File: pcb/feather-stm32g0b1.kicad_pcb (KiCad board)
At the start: 4 copper layers, 50.8 x 22.9 mm, 55 parts, among them CN1 STDC14, CN2 SM04B-SRSS-TB (LF)(SN), CN3 ZX-PH2.0-WT2P, CN4 SM04B-SRSS-TB (LF)(SN), J1 Conn_01x12, J2 Conn_01x16, J3 GT-USB-7010ASV, Q1 DMG3415U-7, SW1 SW_Push, U1 STM32G0B1CBT6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

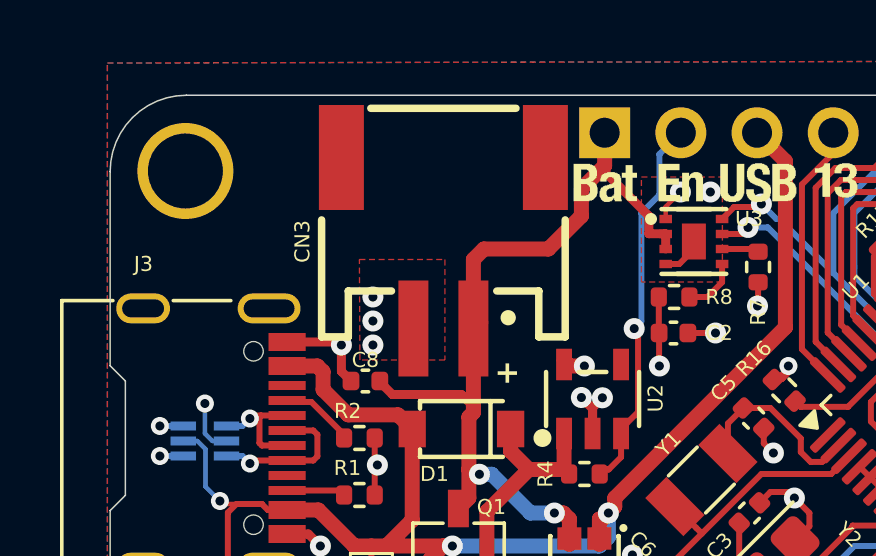
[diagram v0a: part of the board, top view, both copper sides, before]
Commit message: Upgraded kicad project to kicad 10
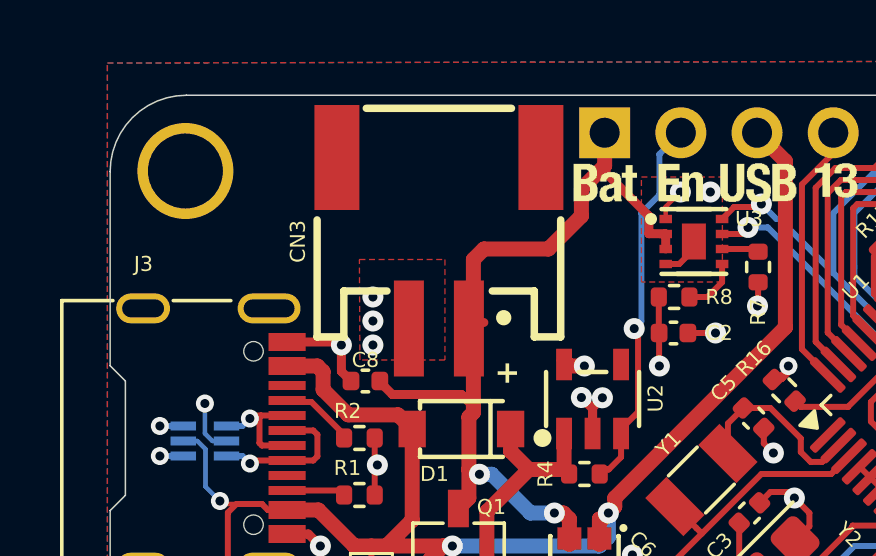
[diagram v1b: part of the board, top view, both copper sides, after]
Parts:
- moved CN3 0.15 mm to (111.0, 84.4)

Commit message: Used kibuzzard to generate nice labels for buttons, ports and leds
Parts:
- added kibuzzard-69DFDE44: G***, kibuzzard-69DFDE44, F.Cu at (134.2, 94.2)
- added kibuzzard-69DFDEC0: G***, kibuzzard-69DFDEC0, F.Cu at (141.8, 96.3)
- added kibuzzard-69DFDEEF: G***, kibuzzard-69DFDEEF, F.Cu at (141.7, 98.0)
- added kibuzzard-69DFDF04: G***, kibuzzard-69DFDF04, F.Cu at (102.1, 97.0)
- added kibuzzard-69DFDF67: G***, kibuzzard-69DFDF67, F.Cu at (140.6, 94.7)
- added kibuzzard-69DFDFA3: G***, kibuzzard-69DFDFA3, F.Cu at (106.3, 84.9)
- added kibuzzard-69DFDFE1: G***, kibuzzard-69DFDFE1, F.Cu at (146.7, 83.8)
- added kibuzzard-69DFDFEF: G***, kibuzzard-69DFDFEF, F.Cu at (146.7, 91.0)
- added kibuzzard-69DFE014: G***, kibuzzard-69DFE014, F.Cu at (141.6, 83.7)
- added kibuzzard-69DFE1A1: G***, kibuzzard-69DFE1A1, F.Cu at (136.8, 98.2)
- SW1: footprint Button_Switch_SMD:SW_SPST_B3U-1000P -> prop-devboard:WUERTH_434153017835
- moved C8 9.26 mm to (116.9, 84.9), turned to 90 degrees
- moved C10 4.79 mm to (131.2, 97.6), turned to 90 degrees
- moved R3 0.90 mm to (129.7, 97.6)
- moved SW1 0.35 mm to (134.2, 96.2), turned to 0 degrees
- moved R10 0.30 mm to (138.7, 98.0)
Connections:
- SW1 pad 1: GND -> NRST
- SW1 pad 2: NRST -> GND
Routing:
- net GND: track 48.4 -> 46.3 mm, vias 33 -> 34
- net VBAT: track 29.1 -> 27.1 mm
- net LED_USR: track 11.2 -> 12.8 mm
- net +3V3: track 112.2 -> 111.5 mm
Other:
- board text removed: "CHRG"
- board text removed: "I2C1"
- board text removed: "I2C2"
- board text removed: "I2C3"
- board text removed: "PWR"
- board text removed: "RESET"
- board text removed: "SPI2"
- board text removed: "USR"

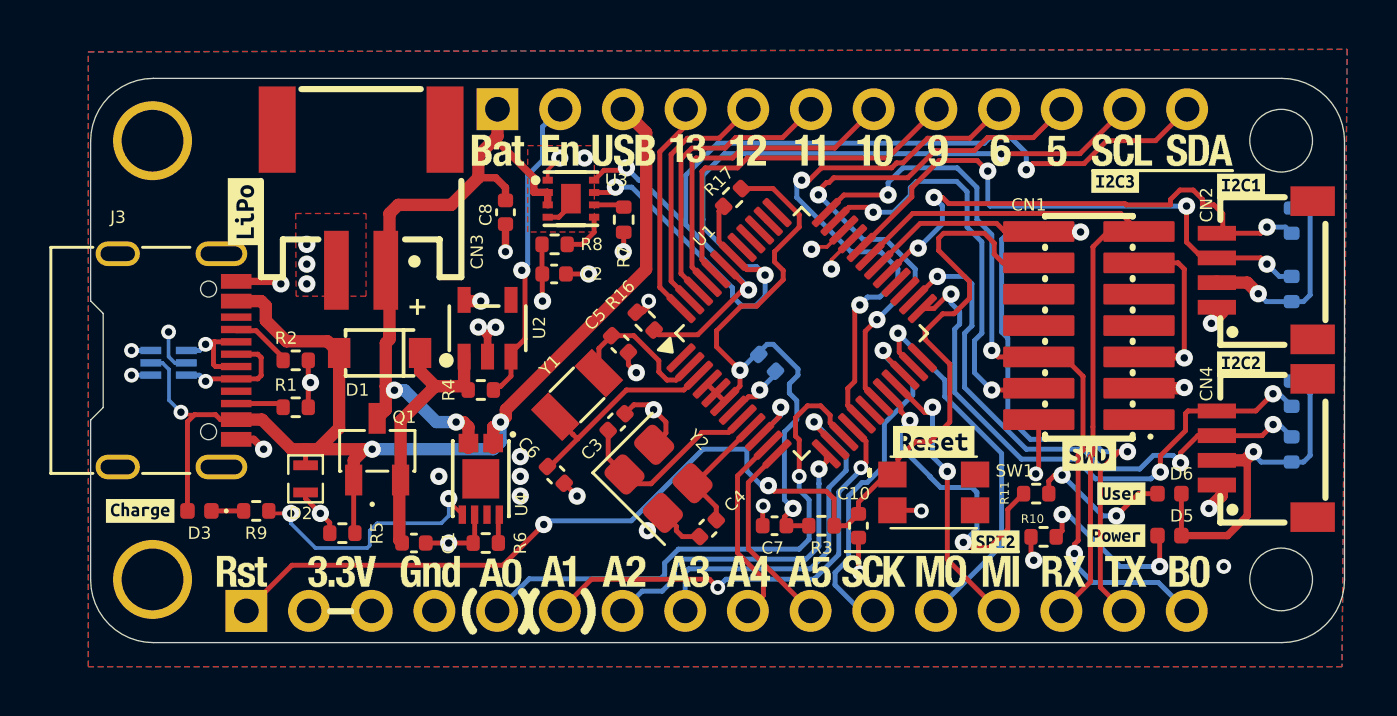
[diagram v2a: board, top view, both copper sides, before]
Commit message: Added I2C EEPROM to the board
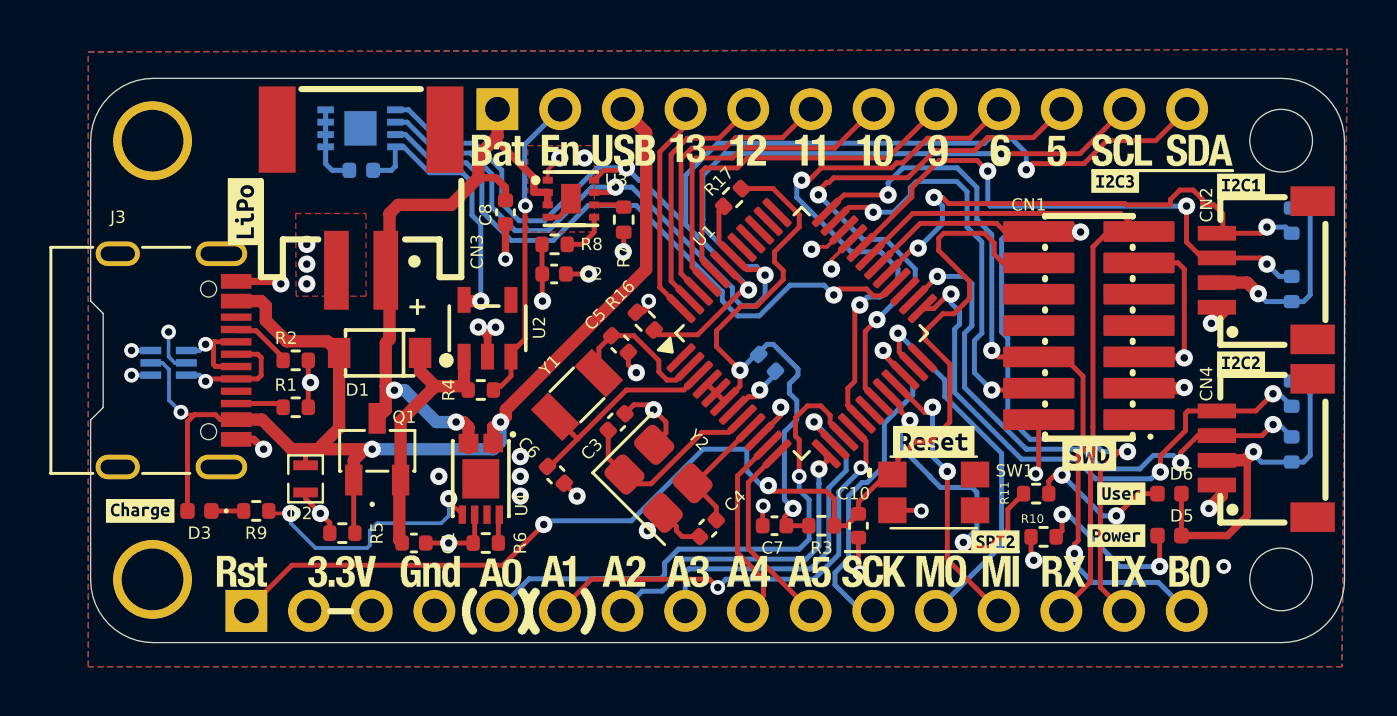
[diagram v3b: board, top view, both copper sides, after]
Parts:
- added C11: 100nF, Capacitor_SMD:C_0402_1005Metric, B.Cu at (111.1, 83.2)
- added U5: M24512-DFMC6TG, prop-devboard:DFN-8_L3.0-W2.0-P0.50-BL-EP, B.Cu at (111.0, 81.5)
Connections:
- U1 pad 28: unconnected-(U1-PA8-Pad28) -> EEPROM_WE
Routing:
- net EEPROM_WE: track 0.00 -> 26.6 mm, vias 0 -> 1
- net I2C3_SDA: track 39.5 -> 52.4 mm
- net I2C3_SCL: track 37.8 -> 50.3 mm
- net +3V3: track 111.5 -> 121.9 mm
- net GND: track 46.3 -> 49.9 mm
